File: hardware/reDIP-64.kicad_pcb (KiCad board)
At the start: 6 copper layers, 25.4 x 50.8 mm, 136 parts, among them J1 USB_C_Receptacle, J2 Conn_01x20, J3 Conn_01x20, J4 Conn_01x20, J5 Conn_01x20, J6 Conn_01x20, J7 Conn_02x05_Odd_Even, Q1 PDTA143ZMB, SW1 KXT331LHS, U1 FUSB340, U10 NCP163AMX120TBG, U11 NCP163AMX250TBG, U12 NCP163AMX300TBG, U13 SN74CBTD16211DGVR, U14 SN74CBTD16211DGVR, U15 SN74CBTD16211DGVR, U16 SN74CBTD16211DGVR, U17 W957A8MFYA5I, U18 W25Q128JVPIM, U19 SGTL5000XNLA3, U2 FSUSB42UMX, U3 PTN5110DHQ, U4 LFE5UM5G-25F-8MG285C, U5 DSC1103CE2-135.0000, U6 FPF1048, U7 FPF2195, U8 MYRGP330100W21RA, U9 MYRGP120100W21RA

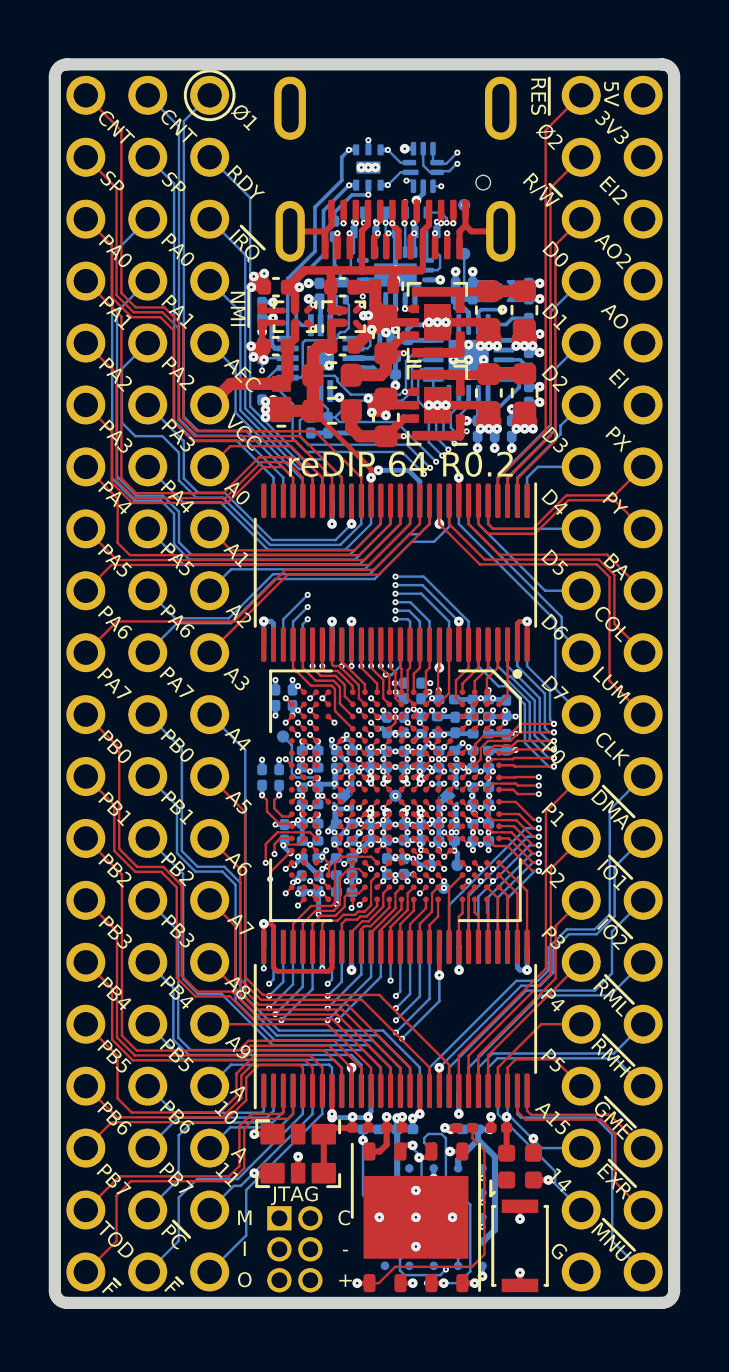
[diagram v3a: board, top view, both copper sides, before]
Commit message: Revision 1.0
* USB receptacle replaced with GCT USB4080-03-A / HRO TYPE-C-31-M-05
* USB PD TCPC changed to PTN5110NHQ (FPF2286 has 15ms VBUS debounce time)
* Complete rework of power section
  - Over-voltage protection on VBUS (FPF2286 / FPF2495C)
  - Bidirectional VCC (2 x TPS22916)
  - Replaced EOLed buck converters with FAN53610 / FAN53611
  - Replaced EOLed LDO for ECP5 VCCAUX with NCP115AMX250TCG
  - Replaced LDO for SGTL5000 VDDA with 3.3V version
  - Added separate LDO for SGTL5000 VDDD, avoiding overvoltage on ECP5 VCC
* Bus switch changed to SN74CBT16211A, biased for level shifting
* Registered I/O for FLASH / HyperRAM clock
* Pin header changes:
  - Machined (round) pins for MOS6510 socket
  - Top only headers for additional I/O
  - Reworked pinout for VIC-II and SID
  - Removed 5V output (now available on bidirectional VCC)
  - Added GND for audio / 3.3V
  - Changed JTAG pinout to match Tag-Connect TC-LATTICE / TC-XILINX6
* Removed EXT_IN capacitors
* Button force changed from 240gf to 100gf
* Space for UL and date codes
* Black solder mask
* Silk screen updates
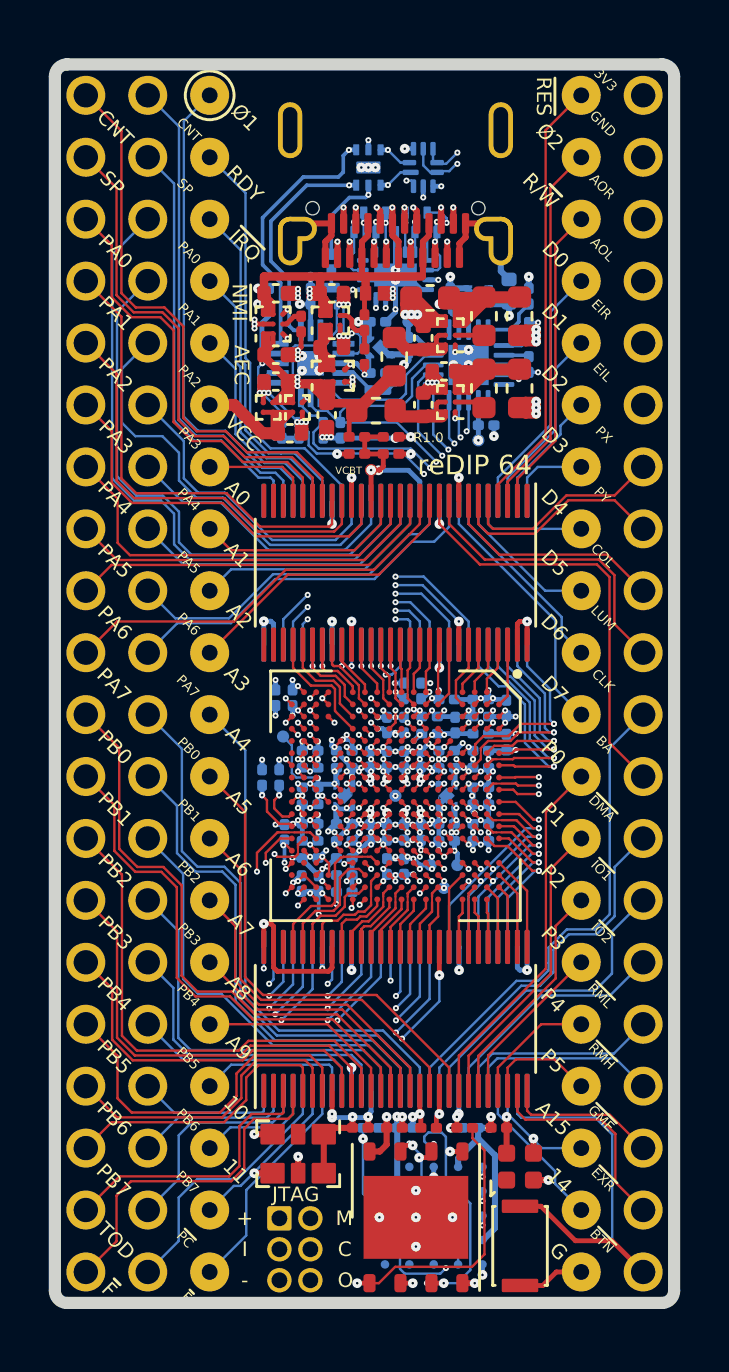
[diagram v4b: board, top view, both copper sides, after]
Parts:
- removed the C35 at (111.5, 112.2)
- removed the C38 at (113.1, 108.0)
- removed the C62 at (113.1, 110.9)
- removed the C63 at (111.7, 113.7)
- removed the C65 at (110.1, 108.0)
- removed the D4 at (102.9, 112.5)
- removed the J3 at (94.9, 100.0)
- removed the TP1 at (110.4, 104.5)
- added C14: 1uF, Capacitor_SMD:C_0402_1005Metric, F.Cu at (105.0, 110.3)
- added C16: 1uF, Capacitor_SMD:C_0402_1005Metric, F.Cu at (102.7, 111.7)
- added C17: 1uF, Capacitor_SMD:C_0402_1005Metric, F.Cu at (103.3, 113.9)
- added C22: 10uF, Capacitor_SMD:C_0402_1005Metric, F.Cu at (109.6, 111.3)
- added C27: 1uF, Capacitor_SMD:C_0402_1005Metric, B.Cu at (112.3, 108.0)
- added C29: 1uF, Capacitor_SMD:C_0201_0603Metric, B.Cu at (106.9, 109.3)
- added C30: 1uF, Capacitor_SMD:C_0201_0603Metric, B.Cu at (108.2, 110.2)
- added C59: 0.1uF, Capacitor_SMD:C_0201_0603Metric, F.Cu at (107.4, 114.7)
- added L1: 1uH, Inductor_SMD:L_0603_1608Metric, F.Cu at (111.2, 109.1)
- added L2: 470nH, Inductor_SMD:L_0603_1608Metric, F.Cu at (111.2, 112.0)
- added R15: 3.83k, Resistor_SMD:R_0201_0603Metric, F.Cu at (106.3, 109.3)
- added R16: 1k, Resistor_SMD:R_0201_0603Metric, F.Cu at (106.3, 110.7)
- added R18: 1k, Resistor_SMD:R_0201_0603Metric, F.Cu at (106.0, 114.0)
- added R19: NC, Resistor_SMD:R_0201_0603Metric, F.Cu at (107.4, 114.0)
- added R20: 6.2k, Resistor_SMD:R_0201_0603Metric, F.Cu at (106.0, 114.7)
- added TP6: TestPoint, reDIP:TestPoint_Pad_D0.5mm, B.Cu at (108.2, 109.3)
- added TP7: TestPoint, reDIP:TestPoint_Pad_D0.5mm, F.Cu at (106.6, 115.4)
- added U10: FPF2495C, ONSemi:CASE_567RV_1.21x1.21mm_P0.4mm, F.Cu at (102.6, 109.4)
- added U11: TPS22916CN, TI:Texas_DSBGA-4_0.78x0.78mm_Layout2x2_P0.4mm, F.Cu at (102.4, 112.8)
- added U12: FAN53611, ONSemi:CASE_567RQ_1.16x0.86mm_P0.4mm, F.Cu at (109.9, 112.6)
- added U16: NCP163AMX120TBG, ONSemi:CASE_711AJ_1.0x1.0mm_P0.65mm, B.Cu at (107.0, 110.3)
- C12: renamed from C32; value 4.7uF -> 2.2uF; footprint Capacitor_SMD:C_0603_1608Metric -> Capacitor_SMD:C_0402_1005Metric
- C21: renamed from C33; value 4.7uF -> 2.2uF; footprint Capacitor_SMD:C_0603_1608Metric -> Capacitor_SMD:C_0402_1005Metric
- C60: moved to F.Cu
- D1: value NSPU3051 -> ESD7241; footprint ONSemi:CASE714AB_1.0x0.6mm -> ONSemi:CASE_714AB_1.0x0.6mm
- J1: value USB_C_Receptacle -> USB4080; footprint JAE:USB_C_Receptacle_JAE_DX07S024JA1 -> GCT:USB_C_Receptacle_GCT_USB4080
- J2: footprint reDIP:PinHeader_1x20_P2.54mm_Vertical -> reDIP:PinHeader_1x20_P2.54mm_Vertical_Machined
- J3: renamed from J6; footprint reDIP:PinHeader_1x20_P2.54mm_Vertical -> reDIP:PinHeader_1x20_P2.54mm_Vertical_Machined
- J4: footprint reDIP:PinHeader_1x20_P2.54mm_Vertical_LongTail -> reDIP:PinHeader_1x20_P2.54mm_Vertical; moved to F.Cu
- J5: value Conn_01x20 -> Conn_02x20_Odd_Even; footprint reDIP:PinHeader_1x20_P2.54mm_Vertical_LongTail -> reDIP:PinHeader_2x20_P2.54mm_Vertical; moved to F.Cu
- R17: renamed from R15; value 453 -> 1.07k
- SW1: value KXT331LHS -> KXT311LHS; footprint Button_Switch_SMD:SW_SPST_CK_KXT3 -> CK:SW_SPST_CK_KXT3
- U1: renamed from U3; value PTN5110DHQ -> PTN5110NHQ
- U13: renamed from U10; footprint ONSemi:CASE711AJ_1.0x1.0mm_P0.65mm -> ONSemi:CASE_711AJ_1.0x1.0mm_P0.65mm
- U14: renamed from U11; value NCP163AMX250TBG -> NCP115AMX250TCG; footprint ONSemi:CASE711AJ_1.0x1.0mm_P0.65mm -> ONSemi:CASE_711AJ_1.0x1.0mm_P0.65mm
- U15: renamed from U12; value NCP163AMX300TBG -> NCP163AMX330TBG; footprint ONSemi:CASE711AJ_1.0x1.0mm_P0.65mm -> ONSemi:CASE_711AJ_1.0x1.0mm_P0.65mm
- U17: renamed from U13; value SN74CBTD16211DGVR -> SN74CBT16211ADGVR
- U18: renamed from U15; value SN74CBTD16211DGVR -> SN74CBT16211ADGVR
- U19: renamed from U14; value SN74CBTD16211DGVR -> SN74CBT16211ADGVR
- U20: renamed from U16; value SN74CBTD16211DGVR -> SN74CBT16211ADGVR
- U3: renamed from U1; footprint ONSemi:CASE722AB_2.0x2.8mm_P0.4mm -> ONSemi:CASE_722AB_2.0x2.8mm_P0.4mm
- U5: renamed from U2; footprint ONSemi:CASE523BC_1.4x1.8_P0.4mm -> ONSemi:CASE_523BC_1.4x1.8_P0.4mm
- U6: value FPF1048 -> FPF2286; footprint ONSemi:CASE567RM_1.46x0.96mm_P0.5mm -> ONSemi:CASE_567UV_1.30x0.90mm_P0.4mm
- U7: value FPF2195 -> FPF1048; footprint ONSemi:CASE567RN_1.48x0.98mm_P0.5mm -> ONSemi:CASE_567RM_1.46x0.96mm_P0.5mm
- U8: value MYRGP330100W21RA -> TPS22916CN; footprint Murata:MYRGP-2.0x2.5mm -> TI:Texas_DSBGA-4_0.78x0.78mm_Layout2x2_P0.4mm
- U9: value MYRGP120100W21RA -> FAN53610; footprint Murata:MYRGP-2.0x2.5mm -> ONSemi:CASE_567RQ_1.16x0.86mm_P0.4mm
- moved C60 32.3 mm to (109.0, 142.3), turned to 0 degrees
- moved TP5 7.67 mm to (111.0, 114.2)
- moved U8 6.72 mm to (103.6, 112.8), turned to 90 degrees
- moved J1 3.95 mm to (107.6, 106.0)
- moved R3 3.35 mm to (103.0, 113.7), turned to 90 degrees
- moved U9 2.92 mm to (109.9, 109.8)
- moved C15 2.89 mm to (104.8, 113.1), turned to -90 degrees
- moved U7 2.87 mm to (105.0, 111.5), turned to 90 degrees
- moved C70 2.72 mm to (113.1, 111.0)
- moved FB1 2.66 mm to (107.6, 110.7), turned to -90 degrees
- moved C69 2.63 mm to (113.1, 109.6)
- moved J5 2.54 mm to (94.9, 100.0), turned to 0 degrees
- moved C18 2.46 mm to (109.0, 108.3), turned to 180 degrees
- moved R4 2.18 mm to (103.7, 113.7)
- moved FB3 1.80 mm to (106.8, 112.9)
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- renumbered C8 to C1, C5 to C10, C6 to C11, C18 to C15, C34 to C18, C12 to C19, C9 to C2, C19 to C20, C36 to C23, C39 to C24, C37 to C25, C40 to C26, C41 to C28, C10 to C3, C21 to C31, C23 to C32, C25 to C33, C27 to C34, C28 to C35, C30 to C36, C14 to C37, C15 to C38, C16 to C39, C7 to C4, C17 to C40, C20 to C41, C22 to C42, C24 to C43, C26 to C44, C29 to C45, C31 to C46, C50 to C47, C52 to C48, C42 to C49, C1 to C5, C44 to C50, C46 to C51, C48 to C52, C43 to C53, C45 to C54, C47 to C55, C49 to C56, C51 to C57, C53 to C58, C11 to C6, C58 to C61, C59 to C62, C55 to C63, C57 to C64, C56 to C65, C54 to C66, C64 to C67, C61 to C68, C66 to C69, C2 to C7, C67 to C70, C3 to C8, C4 to C9, D5 to D4, FB3 to FB2, FB2 to FB3, J7 to J6, R13 to R1, R5 to R10, R8 to R11, R10 to R12, R12 to R13, R9 to R14, R14 to R2, R16 to R21, R18 to R22, R22 to R23, R20 to R24, R17 to R25, R19 to R26, R21 to R27, R6 to R3, R7 to R4, R1 to R5, R2 to R6, R3 to R7, R11 to R8, R4 to R9, TP3 to TP1, TP4 to TP2, TP5 to TP3, TP6 to TP4, TP7 to TP5, TP2 to TP8, U4 to U2, U17 to U21, U18 to U22, U19 to U23, U5 to U4
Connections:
- net /FPGA_IO/I1_~{PC}_TOD renamed /FPGA_IO/I1_TOD
- net /FPGA_IO/I_~{MENU} renamed /FPGA_IO/I_~{BTN}
- C12 pad 1: Net-(C32-Pad1) -> Net-(C12-Pad1)
- C18 pad 1: Net-(C34-Pad1) -> Net-(C18-Pad1)
- C20 pad 1: VCC -> +5V
- C21 pad 1: Net-(C33-Pad1) -> Net-(C21-Pad1)
- C28 pad 1: +3V0 -> VDDA
- C60 pad 1: +1V2 -> VCBT
- C67 pad 1: +3V3 -> VDDA
- C69 pad 1: /Audio/AUDIO_OUT_2 -> /Audio/AUDIO_OUT_R
- C69 pad 2: Net-(C66-Pad2) -> Net-(C69-Pad2)
- C70 pad 1: /Audio/AUDIO_OUT -> /Audio/AUDIO_OUT_L
- C70 pad 2: Net-(C67-Pad2) -> Net-(C70-Pad2)
- FB1 pad 1: Net-(C32-Pad1) -> Net-(C12-Pad1)
- FB2 pad 2: Net-(C34-Pad1) -> Net-(C18-Pad1)
- FB3 pad 1: Net-(C33-Pad1) -> Net-(C21-Pad1)
- FB4 pad 2: Net-(C35-Pad1) -> Net-(C22-Pad1)
- J4 pad 1: +5V -> +3V3
- J4 pad 10: /FPGA_IO/COLOR -> /FPGA_IO/SYNC_LUM
- J4 pad 11: /FPGA_IO/SYNC_LUM -> /FPGA_IO/DOT_CLOCK
- J4 pad 12: /FPGA_IO/DOT_CLOCK -> /FPGA_IO/BA
- J4 pad 2: +3V3 -> GND
- J4 pad 20: /FPGA_IO/~{MENU} -> /FPGA_IO/~{BTN}
- J4 pad 3: /Audio/EXT_IN_2 -> /Audio/AUDIO_OUT_R
- J4 pad 4: /Audio/AUDIO_OUT_2 -> /Audio/AUDIO_OUT_L
- J4 pad 5: /Audio/AUDIO_OUT -> /Audio/EXT_IN_R
- J4 pad 6: /Audio/EXT_IN -> /Audio/EXT_IN_L
- J4 pad 9: /FPGA_IO/BA -> /FPGA_IO/COLOR
- J5 pad 1: /FPGA_IO/CIA2_CNT -> /FPGA_IO/CIA1_CNT
- J5 pad 10: /FPGA_IO/CIA2_PA7 -> /FPGA_IO/CIA2_PA2
- J5 pad 11: /FPGA_IO/CIA2_PB0 -> /FPGA_IO/CIA1_PA3
- J5 pad 12: /FPGA_IO/CIA2_PB1 -> /FPGA_IO/CIA2_PA3
- J5 pad 13: /FPGA_IO/CIA2_PB2 -> /FPGA_IO/CIA1_PA4
- J5 pad 14: /FPGA_IO/CIA2_PB3 -> /FPGA_IO/CIA2_PA4
- J5 pad 15: /FPGA_IO/CIA2_PB4 -> /FPGA_IO/CIA1_PA5
- J5 pad 16: /FPGA_IO/CIA2_PB5 -> /FPGA_IO/CIA2_PA5
- J5 pad 17: /FPGA_IO/CIA2_PB6 -> /FPGA_IO/CIA1_PA6
- J5 pad 18: /FPGA_IO/CIA2_PB7 -> /FPGA_IO/CIA2_PA6
- J5 pad 19: /FPGA_IO/CIA2_~{PC} -> /FPGA_IO/CIA1_PA7
- J5 pad 2: /FPGA_IO/CIA2_SP -> /FPGA_IO/CIA2_CNT
- J5 pad 20: /FPGA_IO/CIA2_~{FLAG} -> /FPGA_IO/CIA2_PA7
- J5 pad 3: /FPGA_IO/CIA2_PA0 -> /FPGA_IO/CIA1_SP
- J5 pad 4: /FPGA_IO/CIA2_PA1 -> /FPGA_IO/CIA2_SP
- J5 pad 5: /FPGA_IO/CIA2_PA2 -> /FPGA_IO/CIA1_PA0
- J5 pad 6: /FPGA_IO/CIA2_PA3 -> /FPGA_IO/CIA2_PA0
- J5 pad 7: /FPGA_IO/CIA2_PA4 -> /FPGA_IO/CIA1_PA1
- J5 pad 8: /FPGA_IO/CIA2_PA5 -> /FPGA_IO/CIA2_PA1
- J5 pad 9: /FPGA_IO/CIA2_PA6 -> /FPGA_IO/CIA1_PA2
- J6 pad 1: /Config_Memory/TMS -> +3V3
- J6 pad 2: /Config_Memory/TCK -> /Config_Memory/TMS
- J6 pad 4: GND -> /Config_Memory/TCK
- J6 pad 5: /Config_Memory/TDO -> GND
- J6 pad 6: +3V3 -> /Config_Memory/TDO
- R17 pad 1: Net-(R15-Pad1) -> Net-(R17-Pad1)
- R24 pad 1: Net-(R20-Pad1) -> /Config_Memory/MCLK
- SW1 pad 1: /Config_Memory/~{BTN} -> /FPGA_IO/~{BTN}
- TP5 pad 1: +3V0 -> VDDA
- U1 pad 1: unconnected-(U3-Pad1) -> /USB_DisplayPort/USB_~{FLIP}
- U1 pad 6: /USB_DisplayPort/USB_~{FLIP} -> /Power/EN_VCC
- U15 pad 1: +3V0 -> VDDA
- U15 pad 3: +3V3 -> +5V
- U15 pad 4: +3V3 -> +5V
- U17 pad 10: /FPGA_IO/SYNC_LUM -> /FPGA_IO/BA
- U17 pad 17: +5V -> VCBT
- U17 pad 18: /FPGA_IO/CIA1_CNT -> /FPGA_IO/CIA1_PA3
- U17 pad 20: /FPGA_IO/CIA1_SP -> /FPGA_IO/CIA1_PA2
- U17 pad 21: /FPGA_IO/CIA1_PA0 -> /FPGA_IO/CIA1_PA1
- U17 pad 22: /FPGA_IO/A0 -> /FPGA_IO/CIA1_CNT
- U17 pad 23: /FPGA_IO/CIA1_PA1 -> /FPGA_IO/CIA1_SP
- U17 pad 24: /FPGA_IO/CIA1_PA2 -> /FPGA_IO/CIA1_PA0
- U17 pad 25: /FPGA_IO/CIA1_PA3 -> /FPGA_IO/A0
- U17 pad 32: /FPGA_IO/I1_PA3 -> /FPGA_IO/I_A0
- U17 pad 33: /FPGA_IO/I1_PA2 -> /FPGA_IO/I1_PA0
- U17 pad 34: /FPGA_IO/I1_PA1 -> /FPGA_IO/I1_SP
- U17 pad 35: /FPGA_IO/I_A0 -> /FPGA_IO/I1_CNT
- U17 pad 36: /FPGA_IO/I1_PA0 -> /FPGA_IO/I1_PA1
- U17 pad 37: /FPGA_IO/I1_SP -> /FPGA_IO/I1_PA2
- U17 pad 39: /FPGA_IO/I1_CNT -> /FPGA_IO/I1_PA3
- U17 pad 46: /FPGA_IO/I_SYNC_LUM -> /FPGA_IO/I_BA
- U17 pad 47: /FPGA_IO/I_COLOR -> /FPGA_IO/I_SYNC_LUM
- U17 pad 48: /FPGA_IO/I_BA -> /FPGA_IO/I_COLOR
- U17 pad 7: /FPGA_IO/BA -> /FPGA_IO/COLOR
- U17 pad 9: /FPGA_IO/COLOR -> /FPGA_IO/SYNC_LUM
- U18 pad 17: +5V -> VCBT
- U19 pad 17: +5V -> VCBT
- U19 pad 3: /FPGA_IO/CIA1_~{PC}_TOD -> /FPGA_IO/CIA1_TOD
- U2 pad F1: /FPGA_IO/I_COLOR -> /FPGA_IO/I_SYNC_LUM
- U2 pad F2: /FPGA_IO/I_BA -> /FPGA_IO/I_COLOR
- U2 pad G1: /FPGA_IO/I_SYNC_LUM -> /FPGA_IO/I_BA
- U2 pad L1: /FPGA_IO/I1_CNT -> /FPGA_IO/I1_PA3
- U2 pad M1: /FPGA_IO/I1_SP -> /FPGA_IO/I1_PA2
- U2 pad M2: /FPGA_IO/I1_PA0 -> /FPGA_IO/I1_PA1
- U2 pad N1: /FPGA_IO/I_A0 -> /FPGA_IO/I1_CNT
- U2 pad N2: /FPGA_IO/I1_PA1 -> /FPGA_IO/I1_SP
- U2 pad N3: /FPGA_IO/I1_PA2 -> /FPGA_IO/I1_PA0
- U2 pad N4: /FPGA_IO/I1_PA3 -> /FPGA_IO/I_A0
- U2 pad T17: /Config_Memory/~{BTN} -> /Config_Memory/MCLK
- U2 pad U16: Net-(R20-Pad1) -> /Config_Memory/MCLK
- U20 pad 17: +5V -> VCBT
- U20 pad 2: /FPGA_IO/~{MENU} -> /FPGA_IO/~{BTN}
- U23 pad 1: Net-(C66-Pad2) -> unconnected-(U23-Pad1)
- U23 pad 12: +3V3 -> VDDA
- U23 pad 20: +1V2 -> VDDD
- U23 pad 3: +3V0 -> VDDA
- U23 pad 4: Net-(C67-Pad2) -> unconnected-(U23-Pad4)
- U23 pad 6: unconnected-(U19-Pad6) -> Net-(C69-Pad2)
- U23 pad 7: unconnected-(U19-Pad7) -> Net-(C70-Pad2)
- U23 pad 8: Net-(C62-Pad1) -> /Audio/EXT_IN_R
- U23 pad 9: Net-(C63-Pad1) -> /Audio/EXT_IN_L
- U6 pad A1: +5V -> Net-(C14-Pad1)
- U6 pad B1: +5V -> Net-(C14-Pad1)
- U6 pad C2: /Power/EN_SNK -> Net-(R15-Pad2)
- U7 pad A1: /Power/~{FAULT} -> +5V
- U7 pad A2: /Power/EN_SRC -> Net-(C14-Pad1)
- U7 pad B1: VBUS -> +5V
- U7 pad B2: VCC -> Net-(C14-Pad1)
- U7 pad C1: Net-(R15-Pad1) -> GND
- U7 pad C2: GND -> /Power/EN_SNK
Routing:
- net VCBT: track 0.00 -> 55.1 mm, vias 0 -> 8
- net +5V: track 92.0 -> 52.4 mm, vias 16 -> 9
- net /Config_Memory/~{BTN}: track 25.7 -> 0.00 mm, vias 4 -> 0
- net /FPGA_IO/~{BTN}: track 0.00 -> 17.5 mm
- net /FPGA_IO/CIA1_~{PC}_TOD: track 11.6 -> 0.00 mm
- net /FPGA_IO/CIA1_TOD: track 0.00 -> 11.6 mm
- net /FPGA_IO/~{MENU}: track 11.4 -> 0.00 mm
- net VDDA: track 0.00 -> 10.8 mm, vias 0 -> 4
- net GND: track 157.2 -> 167.2 mm, vias 264 -> 277
- net /Audio/AUDIO_OUT: track 8.93 -> 0.00 mm, vias 2 -> 0
- net /Audio/EXT_IN_2: track 8.53 -> 0.00 mm, vias 2 -> 0
- net /FPGA_IO/BA: track 9.24 -> 17.6 mm
- net /Audio/EXT_IN: track 8.21 -> 0.00 mm, vias 2 -> 0
- net Net-(C66-Pad2): track 8.02 -> 0.00 mm, vias 4 -> 0
- net Net-(C18-Pad1): track 0.00 -> 7.97 mm
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- removed copper zone on In2.Cu, net +5V
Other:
- board text added: "10"
- board text added: "11"
- board text added: "AOL"
- board text added: "AOR"
- board text added: "Date code"
- board text added: "EIL"
- board text added: "EIR"
- board text added: "R1.0"
- board text added: "UL code"
- board text added: "VCBT"
- board text added: "VDDA"
- board text added: "VDDD"
- board text added: "reDIP 64"
- board text added: "~{BTN}"
- board text added: "© 2022 Dag Lem"
- board text removed: "21-06"
- board text removed: "3V0"
- board text removed: "5V"
- board text removed: "A 10"
- board text removed: "A 11"
- board text removed: "AO"
- board text removed: "AO2"
- board text removed: "CK"
- board text removed: "DI"
- board text removed: "DO"
- board text removed: "EI"
- board text removed: "EI2"
- board text removed: "MS"
- board text removed: "reDIP 64 R0.2"
- board text removed: "~{MNU}"
- board text removed: "© 2021 Dag Lem"
